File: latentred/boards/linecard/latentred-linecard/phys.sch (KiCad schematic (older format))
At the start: 382 parts, among them J2 STEWART_SS_74500_024, Q1 SSM6N58NU, Q2 SSM6N58NU, Q3 SSM6N58NU, Q4 SSM6N58NU, Q5 SSM6N58NU, Q6 SSM6N58NU, Q7 SSM6N58NU, Q8 SSM6N58NU, U10 DP83867, U11 DP83867, U12 DP83867, U13 DP83867, U14 DP83867, U15 DP83867, U16 DSC6101CI2A-025.0000, U17 5PB1108CMG, U8 DP83867, U9 DP83867

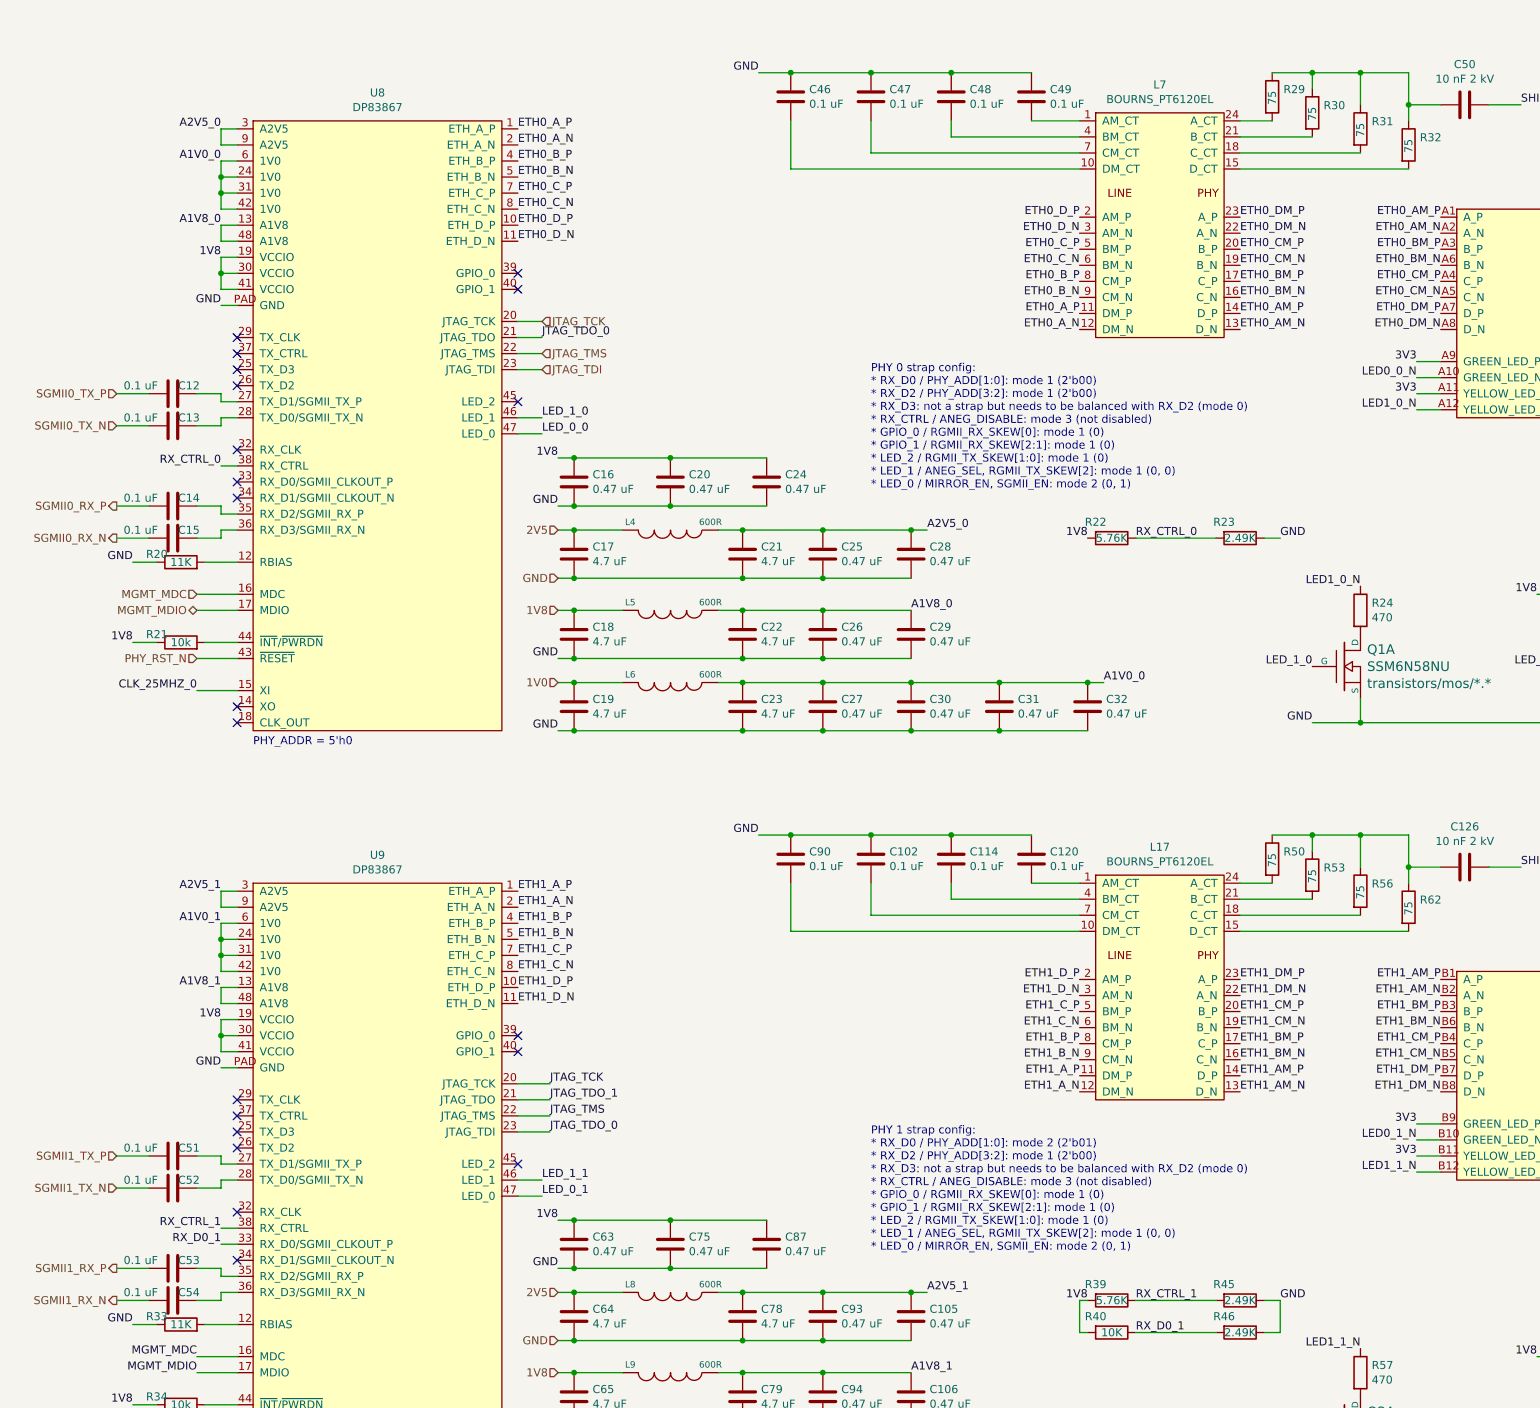
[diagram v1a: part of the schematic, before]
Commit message: Continued PHY layout. Almost done with first pass but have a bunch of tweaking to do.
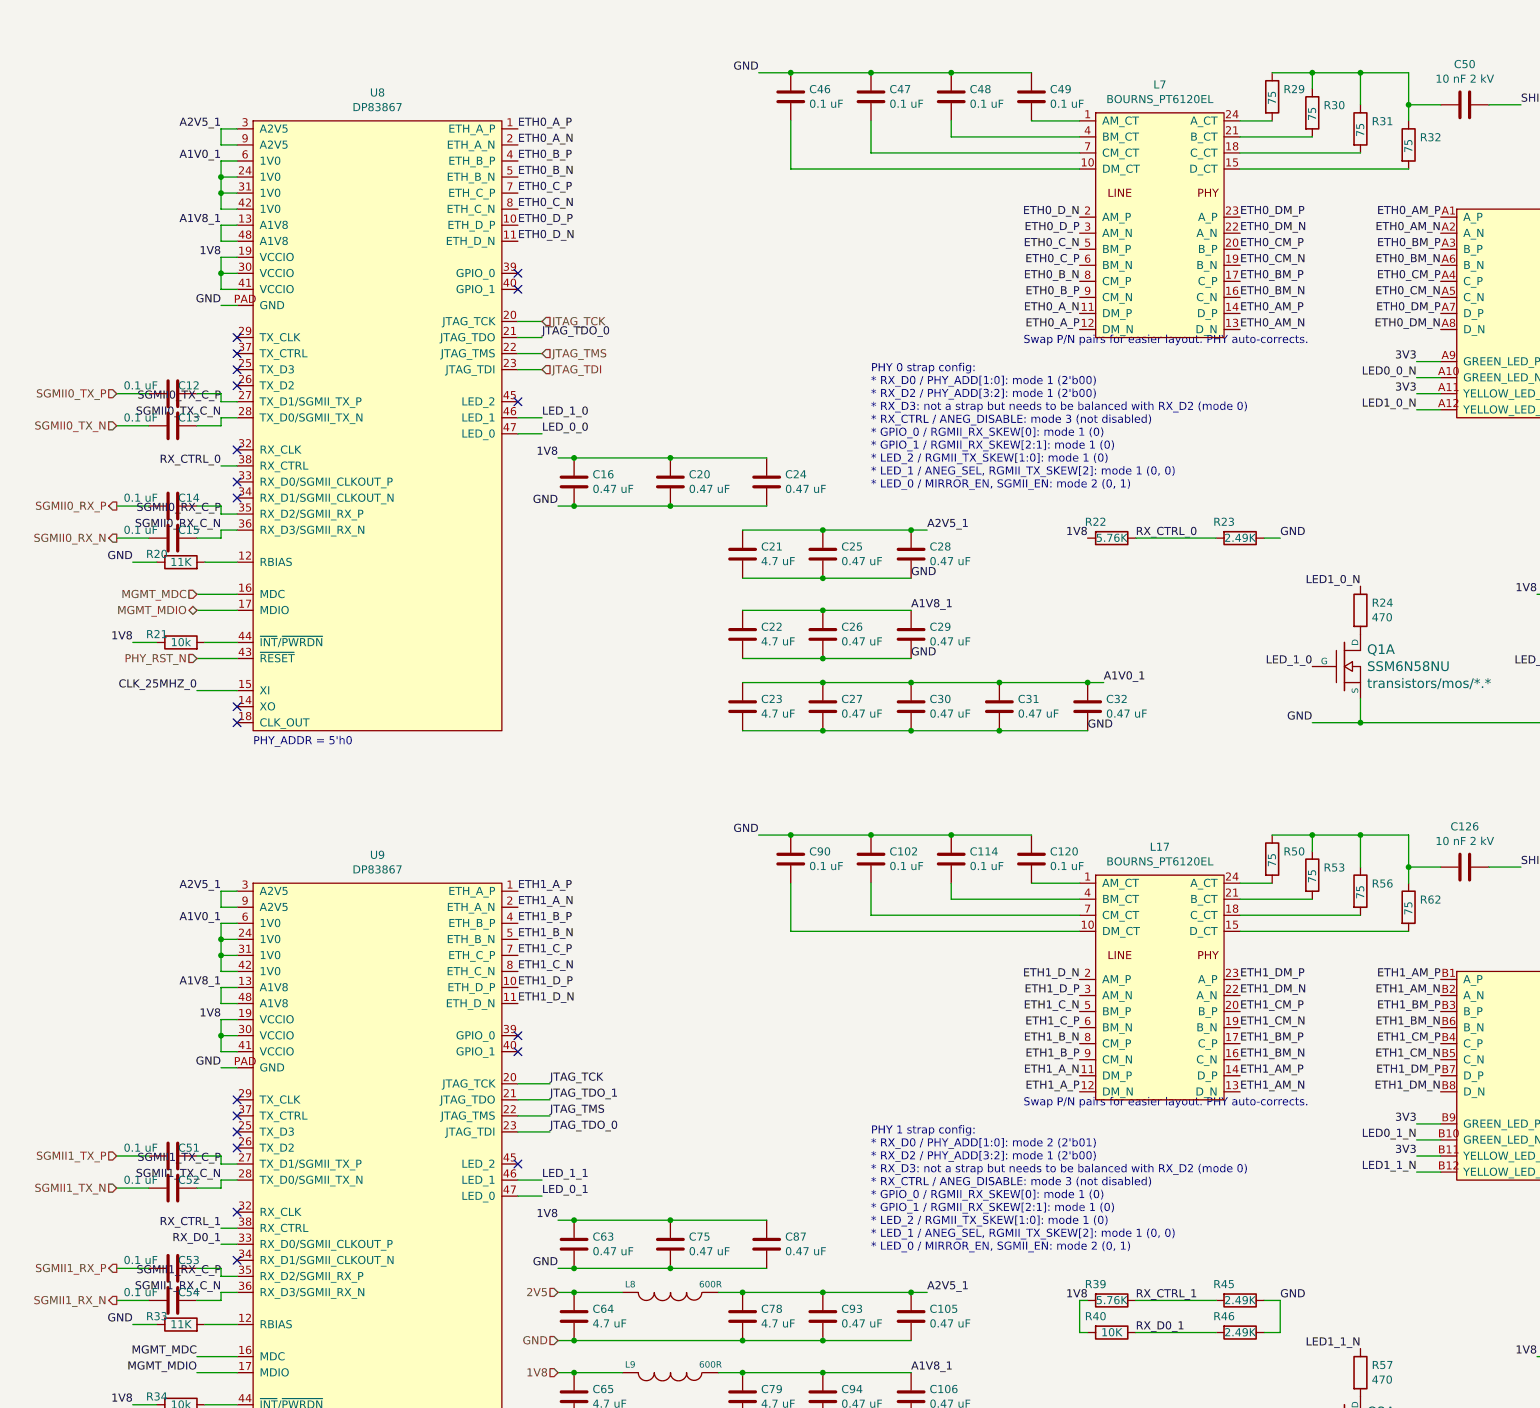
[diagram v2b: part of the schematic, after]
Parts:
- removed C17, C18, C19: 4.7 uF, azonenberg_pcb:EIA_0603_CAP_NOSILK, symbol device:C
- removed L4, L5, L6: 600R, azonenberg_pcb:EIA_0402_RES_NOSILK, symbol passive-azonenberg:INDUCTOR_PWROUT
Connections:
- net A1V0_0 is gone; now on net A1V0_1: C23.1, C27.1, C30.1, C31.1, C32.1, U8.24 (1V0), U8.31 (1V0), U8.42 (1V0), U8.6 (1V0)
- net A1V8_0 is gone; now on net A1V8_1: C22.1, C26.1, C29.1, U8.13 (A1V8), U8.48 (A1V8)
- net A2V5_0 is gone; now on net A2V5_1: C21.1, C25.1, C28.1, U8.3 (A2V5), U8.9 (A2V5)
- net ETH0_A_N: now also L7.11 (DM_P); no longer L7.12 (DM_N)
- net ETH0_A_P: now also L7.12 (DM_N); no longer L7.11 (DM_P)
- net ETH0_B_N: now also L7.8 (CM_P); no longer L7.9 (CM_N)
- net ETH0_B_P: now also L7.9 (CM_N); no longer L7.8 (CM_P)
- net ETH0_C_N: now also L7.5 (BM_P); no longer L7.6 (BM_N)
- net ETH0_C_P: now also L7.6 (BM_N); no longer L7.5 (BM_P)
- net ETH0_D_N: now also L7.2 (AM_P); no longer L7.3 (AM_N)
- net ETH0_D_P: now also L7.3 (AM_N); no longer L7.2 (AM_P)
- net ETH1_A_N: now also L17.11 (DM_P); no longer L17.12 (DM_N)
- net ETH1_A_P: now also L17.12 (DM_N); no longer L17.11 (DM_P)
- net ETH1_B_N: now also L17.8 (CM_P); no longer L17.9 (CM_N)
- net ETH1_B_P: now also L17.9 (CM_N); no longer L17.8 (CM_P)
- net ETH1_C_N: now also L17.5 (BM_P); no longer L17.6 (BM_N)
- net ETH1_C_P: now also L17.6 (BM_N); no longer L17.5 (BM_P)
- net ETH1_D_N: now also L17.2 (AM_P); no longer L17.3 (AM_N)
- net ETH1_D_P: now also L17.3 (AM_N); no longer L17.2 (AM_P)
- net SGMII0_TX_C_P: now reaches C12.1, U8.27 (TX_D1/SGMII_TX_P)
- net SGMII0_TX_C_N: now reaches C13.1, U8.28 (TX_D0/SGMII_TX_N)
- net SGMII0_RX_C_P: now reaches C14.1, U8.35 (RX_D2/SGMII_RX_P)
- net SGMII0_RX_C_N: now reaches C15.1, U8.36 (RX_D3/SGMII_RX_N)
- net SGMII1_TX_C_P: now reaches C51.1, U9.27 (TX_D1/SGMII_TX_P)
- net SGMII1_TX_C_N: now reaches C52.1, U9.28 (TX_D0/SGMII_TX_N)
- net SGMII1_RX_C_P: now reaches C53.1, U9.35 (RX_D2/SGMII_RX_P)
- net SGMII1_RX_C_N: now reaches C54.1, U9.36 (RX_D3/SGMII_RX_N)
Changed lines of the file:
@@
 Sheet 3 3
 Title "LATENTRED 8-port 10/100/1000 Base-T Line Card"
-Date "2018-04-26"
+Date "2018-04-27"
 Rev "0.1"
 Comp "Andrew D. Zonenberg"
@@
 Text HLabel 3100 5350 0    50   Input ~ 0
 MGMT_MDC
-Text HLabel 5350 5250 0    50   Input ~ 0
-GND
-Text HLabel 5350 5900 0    50   Input ~ 0
-1V0
-Text HLabel 5350 5450 0    50   Input ~ 0
-1V8
-Text HLabel 5350 4950 0    50   Input ~ 0
-2V5
 Text HLabel 5250 3950 2    50   Input ~ 0
 JTAG_TDI
@@
 Wire Wire Line
 	3250 3050 3350 3050
-$Comp
-L passive-azonenberg:INDUCTOR_PWROUT L4
-U 1 1 5AFEFEEF
-P 6050 4950
-F 0 "L4" V 6000 4700 40  0000 C CNN
-F 1 "600R" V 6000 5200 40  0000 C CNN
-F 2 "azonenberg_pcb:EIA_0402_RES_NOSILK" H 6050 4950 60  0001 C CNN
-F 3 "" H 6050 4950 60  0000 C CNN
-	1    6050 4950
-	0    1    1    0
-$EndComp
 Text Label 3250 2650 2    50   ~ 0
-A1V0_0
+A1V0_1
 Text Label 3250 3050 2    50   ~ 0
-A1V8_0
-$Comp
-L passive-azonenberg:INDUCTOR_PWROUT L6
-U 1 1 5AFF0369
-P 6050 5900
-F 0 "L6" V 6000 5650 40  0000 C CNN
-F 1 "600R" V 6000 6150 40  0000 C CNN
-F 2 "azonenberg_pcb:EIA_0402_RES_NOSILK" H 6050 5900 60  0001 C CNN
-F 3 "" H 6050 5900 60  0000 C CNN
-	1    6050 5900
-	0    1    1    0
-$EndComp
-$Comp
-L passive-azonenberg:INDUCTOR_PWROUT L5
-U 1 1 5AFF08BE
-P 6050 5450
-F 0 "L5" V 6000 5200 40  0000 C CNN
-F 1 "600R" V 6000 5700 40  0000 C CNN
-F 2 "azonenberg_pcb:EIA_0402_RES_NOSILK" H 6050 5450 60  0001 C CNN
-F 3 "" H 6050 5450 60  0000 C CNN
-	1    6050 5450
-	0    1    1    0
-$EndComp
+A1V8_1
 Text Label 3250 3250 2    50   ~ 0
 1V8
@@
 Wire Wire Line
 	2600 5000 2800 5000
-$Comp
-L device:C C17
-U 1 1 5B00BF06
-P 5450 5100
-F 0 "C17" H 5565 5146 50  0000 L CNN
-F 1 "4.7 uF" H 5565 5055 50  0000 L CNN
-F 2 "azonenberg_pcb:EIA_0603_CAP_NOSILK" H 5488 4950 50  0001 C CNN
-F 3 "" H 5450 5100 50  0001 C CNN
-	1    5450 5100
-	1    0    0    -1
-$EndComp
 Text Label 3250 2450 2    50   ~ 0
-A2V5_0
+A2V5_1
 $Comp
 L device:C C21
@@
 $EndComp
 Wire Wire Line
-	5350 4950 5450 4950
-Wire Wire Line
-	5450 4950 5750 4950
-Connection ~ 5450 4950
-Wire Wire Line
-	6350 4950 6500 4950
-Wire Wire Line
 	6500 4950 7000 4950
-Connection ~ 6500 4950
 Wire Wire Line
 	7000 4950 7550 4950
@@
 	3250 3550 3350 3550
 Wire Wire Line
-	5350 5250 5450 5250
-Wire Wire Line
-	5450 5250 6500 5250
-Connection ~ 5450 5250
-Wire Wire Line
 	7000 5250 6500 5250
-Connection ~ 6500 5250
 Wire Wire Line
 	7000 5250 7550 5250
 Connection ~ 7000 5250
 $Comp
-L device:C C18
-U 1 1 5B022840
-P 5450 5600
-F 0 "C18" H 5565 5646 50  0000 L CNN
-F 1 "4.7 uF" H 5565 5555 50  0000 L CNN
-F 2 "azonenberg_pcb:EIA_0603_CAP_NOSILK" H 5488 5450 50  0001 C CNN
-F 3 "" H 5450 5600 50  0001 C CNN
-	1    5450 5600
-	1    0    0    -1
-$EndComp
-Wire Wire Line
-	5750 5450 5450 5450
-Wire Wire Line
-	5450 5450 5350 5450
-Connection ~ 5450 5450
-Text Label 5350 5750 2    50   ~ 0
-GND
-Wire Wire Line
-	5350 5750 5450 5750
-$Comp
 L device:C C22
 U 1 1 5B02643D
@@
 $EndComp
 Text Label 7650 4950 0    50   ~ 0
-A2V5_0
+A2V5_1
 Wire Wire Line
 	7650 4950 7550 4950
 Connection ~ 7550 4950
 Text Label 7550 5450 0    50   ~ 0
-A1V8_0
+A1V8_1
 Wire Wire Line
 	7550 5450 7000 5450
-Wire Wire Line
-	6500 5450 6350 5450
-Connection ~ 6500 5450
 $Comp
 L device:C C26
@@
 $EndComp
 Wire Wire Line
-	5450 5750 6500 5750
-Connection ~ 5450 5750
-Wire Wire Line
 	6500 5750 7000 5750
-Connection ~ 6500 5750
 Wire Wire Line
 	7000 5750 7550 5750
 Connection ~ 7000 5750
 $Comp
-L device:C C19
-U 1 1 5B02E776
-P 5450 6050
-F 0 "C19" H 5565 6096 50  0000 L CNN
-F 1 "4.7 uF" H 5565 6005 50  0000 L CNN
-F 2 "azonenberg_pcb:EIA_0603_CAP_NOSILK" H 5488 5900 50  0001 C CNN
-F 3 "" H 5450 6050 50  0001 C CNN
-	1    5450 6050
-	1    0    0    -1
-$EndComp
-Wire Wire Line
-	5750 5900 5450 5900
-Wire Wire Line
-	5350 5900 5450 5900
-Connection ~ 5450 5900
-$Comp
 L device:C C23
 U 1 1 5B0319A3
@@
 Wire Wire Line
 	8650 5900 8100 5900
-Wire Wire Line
-	6350 5900 6500 5900
 Connection ~ 8100 5900
-Connection ~ 6500 5900
 Wire Wire Line
 	6500 5900 7000 5900
@@
 	7550 5900 8100 5900
 Wire Wire Line
-	5450 6200 6500 6200
-Connection ~ 6500 6200
-Wire Wire Line
 	6500 6200 7000 6200
 Connection ~ 7000 6200
@@
 	8100 6200 8650 6200
 Text Label 8750 5900 0    50   ~ 0
-A1V0_0
+A1V0_1
 Wire Wire Line
 	8750 5900 8650 5900
@@
 Text Label 5350 4500 2    50   ~ 0
 1V8
-Text Label 5350 6200 2    50   ~ 0
+Text Label 8650 6200 0    50   ~ 0
 GND
-Wire Wire Line
-	5350 6200 5450 6200
-Connection ~ 5450 6200
 Text Label 5350 4800 2    50   ~ 0
 GND
@@
 Text Label 9600 7850 0    50   ~ 0
 ETH1_DM_N
-Text Label 8600 8350 2    50   ~ 0
-ETH1_A_P
 Text Label 8600 8450 2    50   ~ 0
+ETH1_A_P
+Text Label 8600 8350 2    50   ~ 0
 ETH1_A_N
-Text Label 8600 8150 2    50   ~ 0
-ETH1_B_P
 Text Label 8600 8250 2    50   ~ 0
+ETH1_B_P
+Text Label 8600 8150 2    50   ~ 0
 ETH1_B_N
-Text Label 8600 7950 2    50   ~ 0
-ETH1_C_P
 Text Label 8600 8050 2    50   ~ 0
+ETH1_C_P
+Text Label 8600 7950 2    50   ~ 0
 ETH1_C_N
-Text Label 8600 7750 2    50   ~ 0
-ETH1_D_P
 Text Label 8600 7850 2    50   ~ 0
+ETH1_D_P
+Text Label 8600 7750 2    50   ~ 0
 ETH1_D_N
 Text Label 20500 13150 2    50   ~ 0
@@
 Text Label 8650 12450 2    50   ~ 0
 ETH2_D_N
-Text Label 8600 3600 2    50   ~ 0
-ETH0_A_P
 Text Label 8600 3700 2    50   ~ 0
+ETH0_A_P
+Text Label 8600 3600 2    50   ~ 0
 ETH0_A_N
-Text Label 8600 3400 2    50   ~ 0
-ETH0_B_P
 Text Label 8600 3500 2    50   ~ 0
+ETH0_B_P
+Text Label 8600 3400 2    50   ~ 0
 ETH0_B_N
-Text Label 8600 3200 2    50   ~ 0
-ETH0_C_P
 Text Label 8600 3300 2    50   ~ 0
+ETH0_C_P
+Text Label 8600 3200 2    50   ~ 0
 ETH0_C_N
-Text Label 8600 3000 2    50   ~ 0
-ETH0_D_P
 Text Label 8600 3100 2    50   ~ 0
+ETH0_D_P
+Text Label 8600 3000 2    50   ~ 0
 ETH0_D_N
 Text Label 10850 3000 2    50   ~ 0
@@
 Text Notes 8300 13300 0    50   ~ 0
 Swap P/N pairs for easier layout. PHY auto-corrects.
+Text Notes 8250 8550 0    50   ~ 0
+Swap P/N pairs for easier layout. PHY auto-corrects.
+Text Notes 8250 3800 0    50   ~ 0
+Swap P/N pairs for easier layout. PHY auto-corrects.
+Text Label 7550 5750 0    50   ~ 0
+GND
+Text Label 3250 8900 2    50   ~ 0
+SGMII1_TX_C_P
+Text Label 3250 9000 2    50   ~ 0
+SGMII1_TX_C_N
+Text Label 3250 9600 2    50   ~ 0
+SGMII1_RX_C_P
+Text Label 3250 9700 2    50   ~ 0
+SGMII1_RX_C_N
+Text Label 3250 4150 2    50   ~ 0
+SGMII0_TX_C_P
+Text Label 3250 4250 2    50   ~ 0
+SGMII0_TX_C_N
+Text Label 3250 4850 2    50   ~ 0
+SGMII0_RX_C_P
+Text Label 3250 4950 2    50   ~ 0
+SGMII0_RX_C_N
+Text Label 7550 5250 0    50   ~ 0
+GND
 $EndSCHEMATC
